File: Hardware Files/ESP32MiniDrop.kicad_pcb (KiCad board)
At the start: 2 copper layers, 74 x 54 mm, 33 parts, among them J2 Barrel_Jack, J3 AudioJack3, J4 Solenoid1 Terminal, J5 0.100" 2x4 Header, M1 Conn_01x01, M2 Conn_01x01, M3 Conn_01x01, M4 Conn_01x01, Q3 NMOS 60V 46A, SW1 SPST (RED), SW2 SPST (BLUE), U2 AZ1117-3.3, U3 ESP32-WROOM-32, U4 4N25, U5 4N25

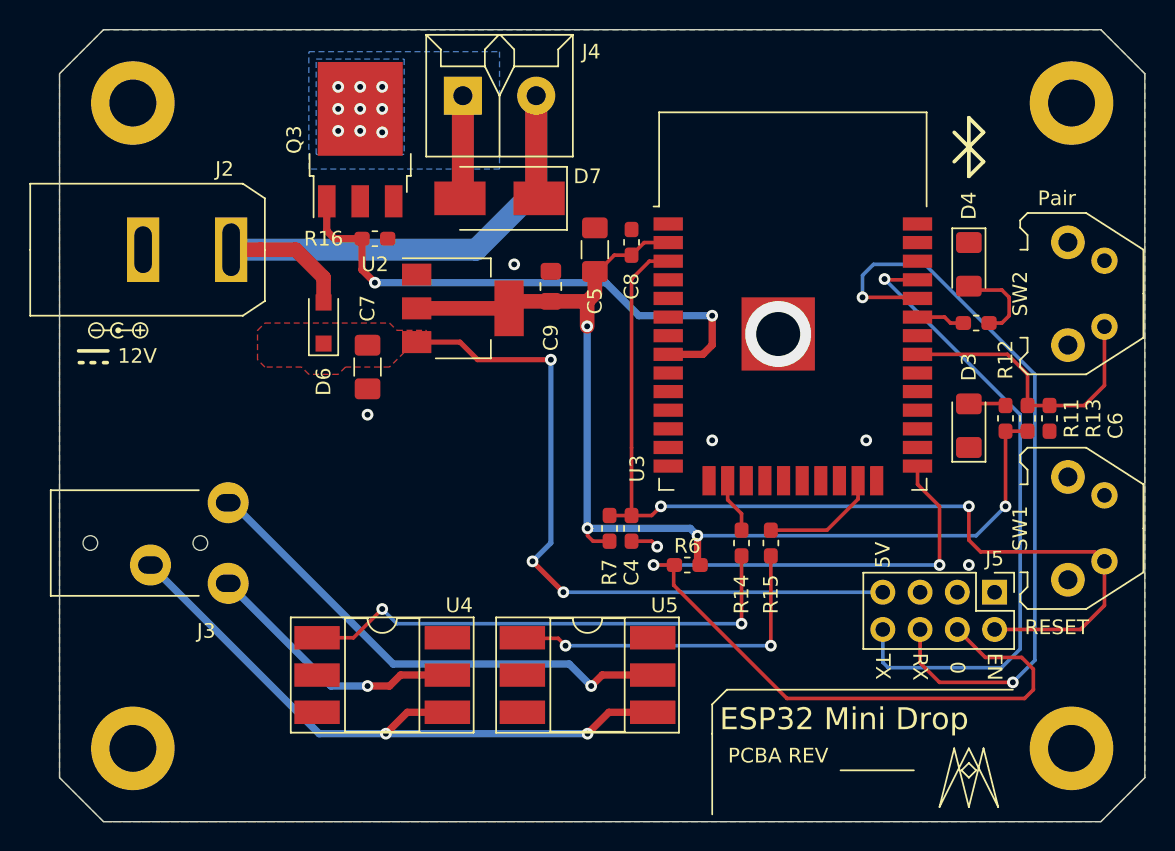
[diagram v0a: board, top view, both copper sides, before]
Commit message: Update passives to all 1206, unroute and reposition
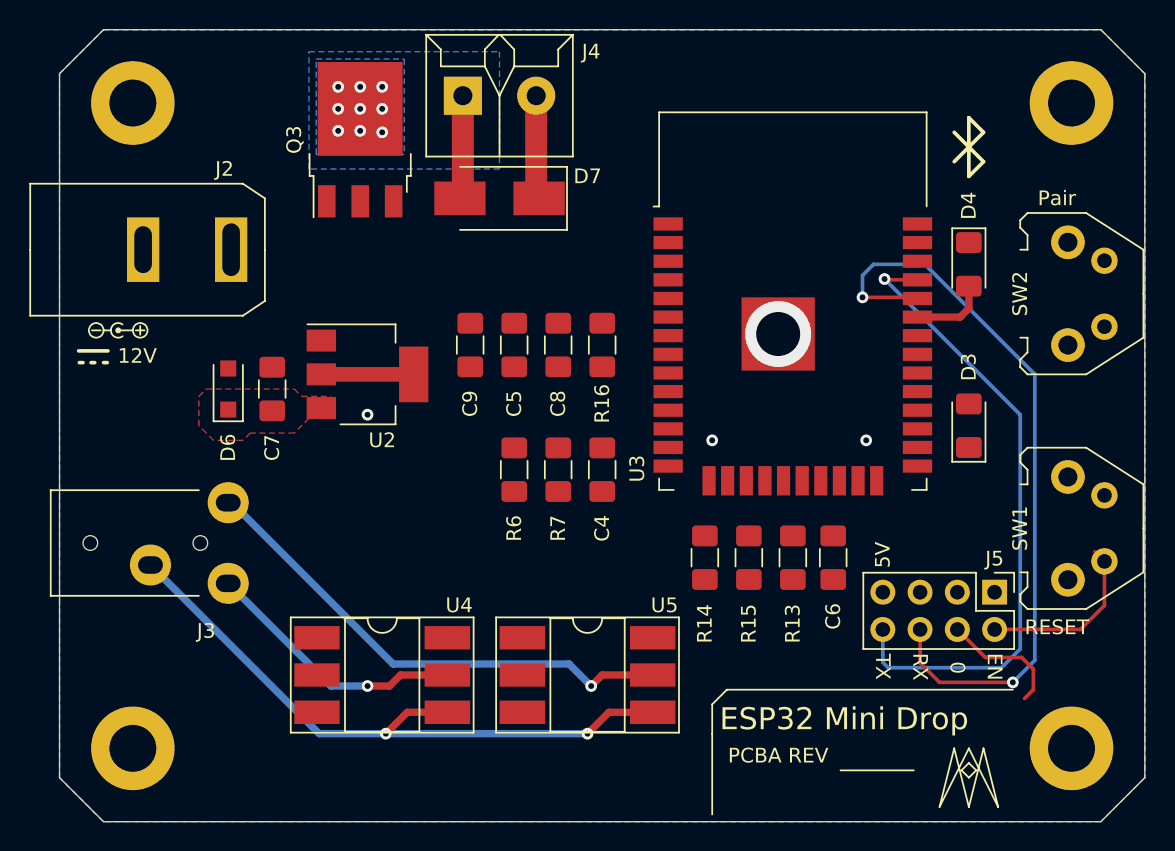
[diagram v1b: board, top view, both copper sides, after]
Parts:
- removed R11, R12: 0R 0.1W, Resistor_SMD:R_0603_1608Metric_Pad1.05x0.95mm_HandSolder
- C4, C6, C8: footprint Capacitor_SMD:C_0603_1608Metric_Pad1.05x0.95mm_HandSolder -> Capacitor_SMD:C_1206_3216Metric_Pad1.42x1.75mm_HandSolder
- C9: footprint Capacitor_SMD:C_0805_2012Metric_Pad1.15x1.40mm_HandSolder -> Capacitor_SMD:C_1206_3216Metric_Pad1.42x1.75mm_HandSolder
- R13, R14, R15, R16, R6, R7: footprint Resistor_SMD:R_0603_1608Metric_Pad1.05x0.95mm_HandSolder -> Resistor_SMD:R_1206_3216Metric_Pad1.42x1.75mm_HandSolder
- moved R13 18.6 mm to (50.0, 36.0)
- moved C6 17.5 mm to (52.8, 36.0)
- moved R16 17.1 mm to (37.0, 21.5), turned to 90 degrees
- moved R6 13.5 mm to (31.0, 30.0), turned to 270 degrees
- moved C8 8.60 mm to (34.0, 21.5)
- moved C5 8.51 mm to (31.0, 21.5)
- moved D6 7.91 mm to (11.5, 24.5)
- moved U2 7.91 mm to (21.0, 23.5)
- moved C9 6.80 mm to (28.0, 21.5)
- moved C7 6.67 mm to (14.5, 24.5), turned to 270 degrees
- moved R7 5.32 mm to (34.0, 30.0), turned to 270 degrees
- moved C4 4.47 mm to (37.0, 30.0), turned to 270 degrees
- moved R14 2.69 mm to (44.0, 36.0)
- moved R15 1.80 mm to (47.0, 36.0)
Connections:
- D3 pad 2: Net-(D3-Pad2) -> +3V3
- D4 pad 2: Net-(D4-Pad2) -> PairLED_CTLO
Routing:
- net +3V3: track 76.0 -> 6.83 mm, vias 4 -> 0
- net /IO0: track 65.4 -> 8.56 mm, vias 2 -> 0
- net /EN: track 67.2 -> 12.1 mm, vias 2 -> 0
- net /VREG_IN: track 49.1 -> 0.30 mm, vias 3 -> 0
- net +12V: track 45.1 -> 7.37 mm
- net Solenoid_1_CTLO: track 37.4 -> 0.00 mm, vias 2 -> 0
- net Net-(R14-Pad1): track 34.8 -> 0.00 mm, vias 2 -> 0
- net Net-(R15-Pad1): track 23.3 -> 0.06 mm, vias 2 -> 0
- net PairSwitch_CTLI: track 20.2 -> 0.16 mm
- net Shutter_CTLO: track 8.07 -> 0.00 mm
- net Net-(D4-Pad2): track 6.05 -> 0.00 mm
- net Focus_CTLO: track 3.76 -> 0.00 mm
- net Net-(D3-Pad2): track 2.56 -> 0.00 mm
- net PairLED_CTLO: track 3.29 -> 5.52 mm
- net GND: track 1.91 -> 0.00 mm, vias 7 -> 4

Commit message: Reroute components
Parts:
- added R1: 10k 1% 0.1W, Resistor_SMD:R_1206_3216Metric_Pad1.42x1.75mm_HandSolder, F.Cu at (40.0, 38.0)
- moved U5 16.9 mm to (22.0, 34.5), turned to 180 degrees
- moved R14 7.28 mm to (37.0, 38.0)
- moved C6 4.47 mm to (48.8, 38.0)
- moved R13 4.47 mm to (46.0, 38.0)
- moved R15 4.47 mm to (43.0, 38.0)
- moved U4 1.00 mm to (22.0, 45.0), turned to 180 degrees
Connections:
- U3 pad 23: Shutter_CTLO -> U0TX_Active
- U3 pad 24: Net-(U3-Pad24) -> Shutter_CTLO
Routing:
- net /EN: track 12.1 -> 83.9 mm, vias 0 -> 3
- net /IO0: track 8.56 -> 80.2 mm, vias 0 -> 4
- net +3V3: track 6.83 -> 78.2 mm, vias 0 -> 7
- net /VREG_IN: track 0.30 -> 71.2 mm, vias 0 -> 2
- net PairSwitch_CTLI: track 0.16 -> 41.7 mm, vias 0 -> 2
- net Solenoid_1_CTLO: track 0.00 -> 31.1 mm
- net Net-(J3-PadT): track 34.4 -> 7.24 mm, vias 1 -> 0
- net U0TX_Active: track 0.00 -> 26.3 mm, vias 0 -> 2
- net Net-(R14-Pad1): track 0.00 -> 21.4 mm, vias 0 -> 2
- net Net-(R15-Pad1): track 0.06 -> 21.1 mm
- net Shutter_CTLO: track 0.00 -> 17.5 mm
- net Net-(J3-PadS): track 44.4 -> 27.4 mm
- net Focus_CTLO: track 0.00 -> 13.5 mm
- net +12V: track 7.37 -> 15.5 mm
- net Net-(J3-PadR): track 18.2 -> 17.5 mm, vias 1 -> 0
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- added copper zone on B.Cu, net +12V
- added copper zone on F.Cu, net +3V3

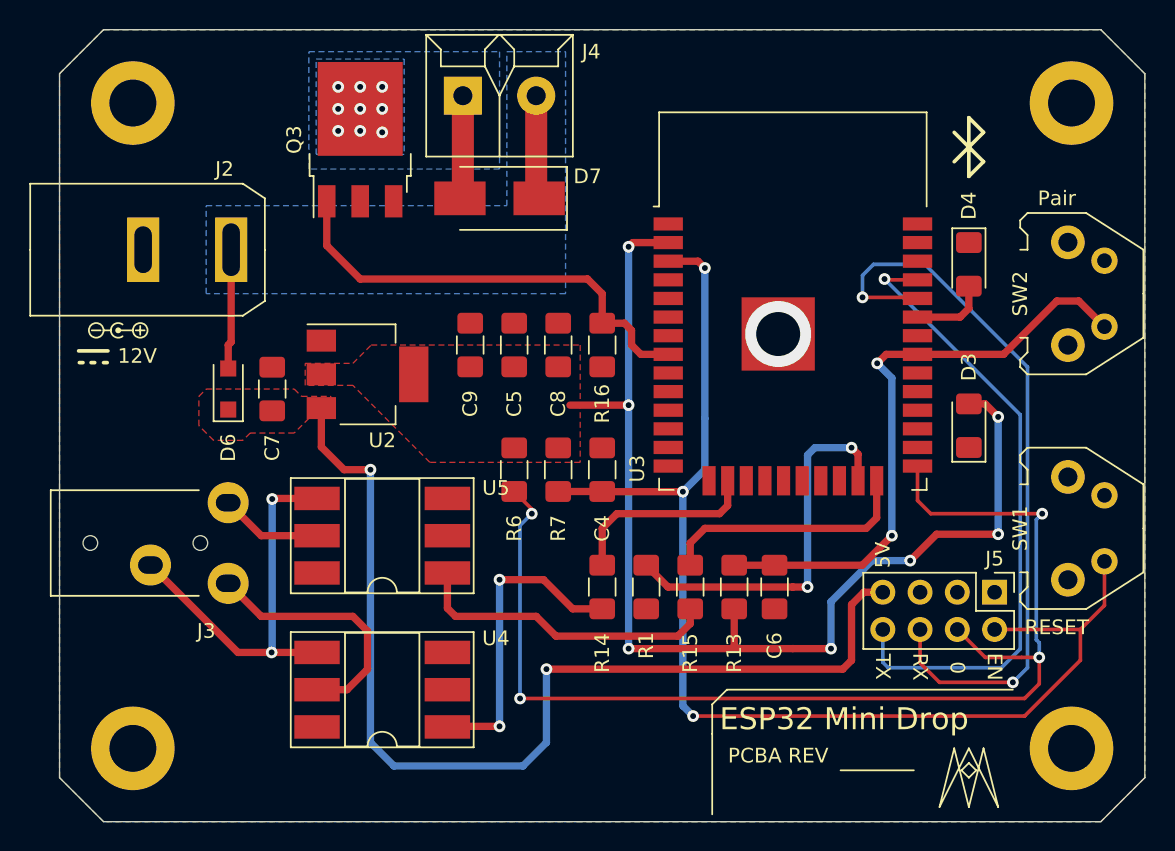
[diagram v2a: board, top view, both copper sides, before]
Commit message: Attach Pair Switch to ESP32 IO0 for boot mode selection
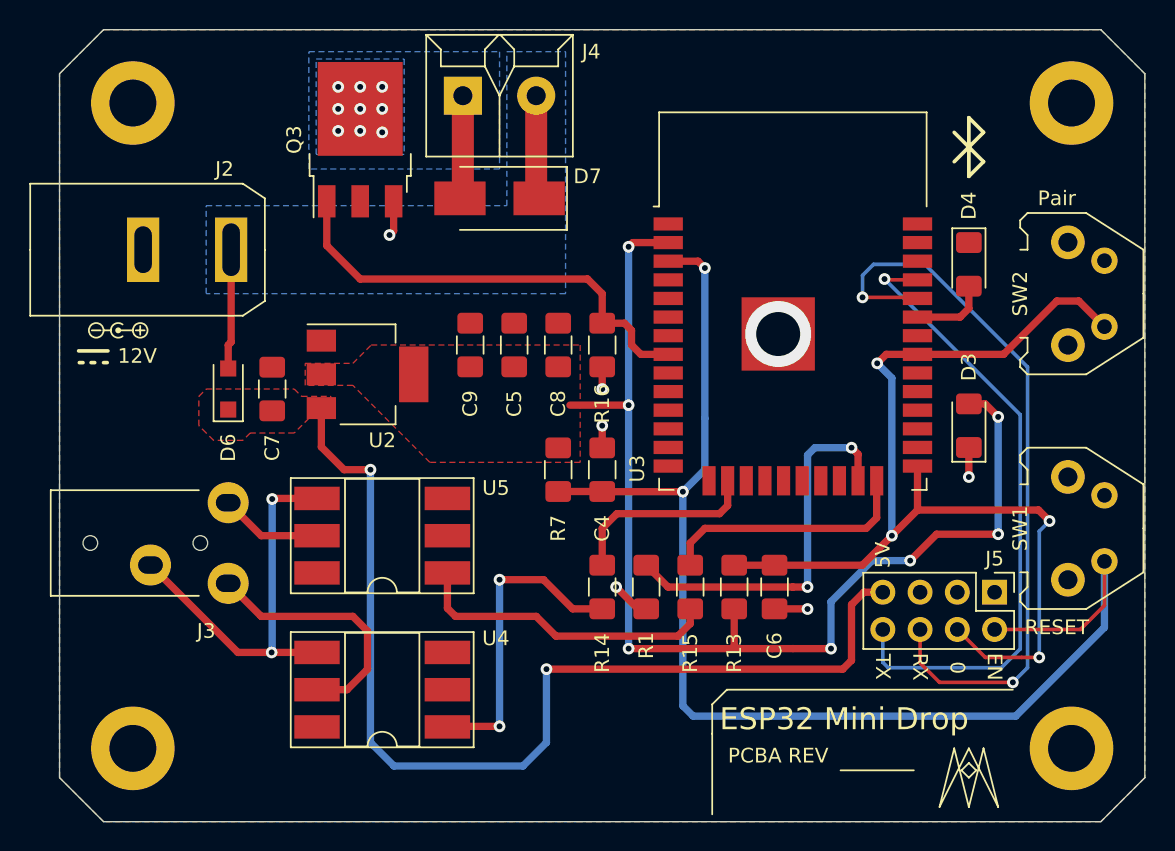
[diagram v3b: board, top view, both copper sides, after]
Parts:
- removed R6: 10k 1% 0.1W, Resistor_SMD:R_1206_3216Metric_Pad1.42x1.75mm_HandSolder
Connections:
- J5 pad 4: /IO0 -> PairSwitch_CTLI
- U3 pad 25: /IO0 -> PairSwitch_CTLI
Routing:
- net /IO0: track 80.2 -> 0.00 mm, vias 4 -> 0
- net PairSwitch_CTLI: track 41.7 -> 74.8 mm, vias 2 -> 4
- net GND: track 0.00 -> 12.4 mm, vias 1 -> 7
- net /EN: track 83.9 -> 88.9 mm, vias 3 -> 2

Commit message: Update Component MPN and Values
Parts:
- removed C9: 22uF 6.3V, Capacitor_SMD:C_1206_3216Metric_Pad1.42x1.75mm_HandSolder
- C2: renamed from C5; value 10uF 50V -> 10uF 25V 10%
- C5: renamed from C7; value 10uF 50V -> 10uF 25V 10%
- renumbered C4 to C1, C8 to C3, C6 to C4, D3 to D1, D4 to D2, D7 to D3, D6 to D4, J5 to J1, J4 to J2, J2 to J4, Q3 to Q1, R7 to R1, R13 to R2, R1 to R3, R14 to R4, R16 to R5, R15 to R6, SW2 to SW1, SW1 to SW2, U3 to U1, U4 to U2, U5 to U3, U2 to U4

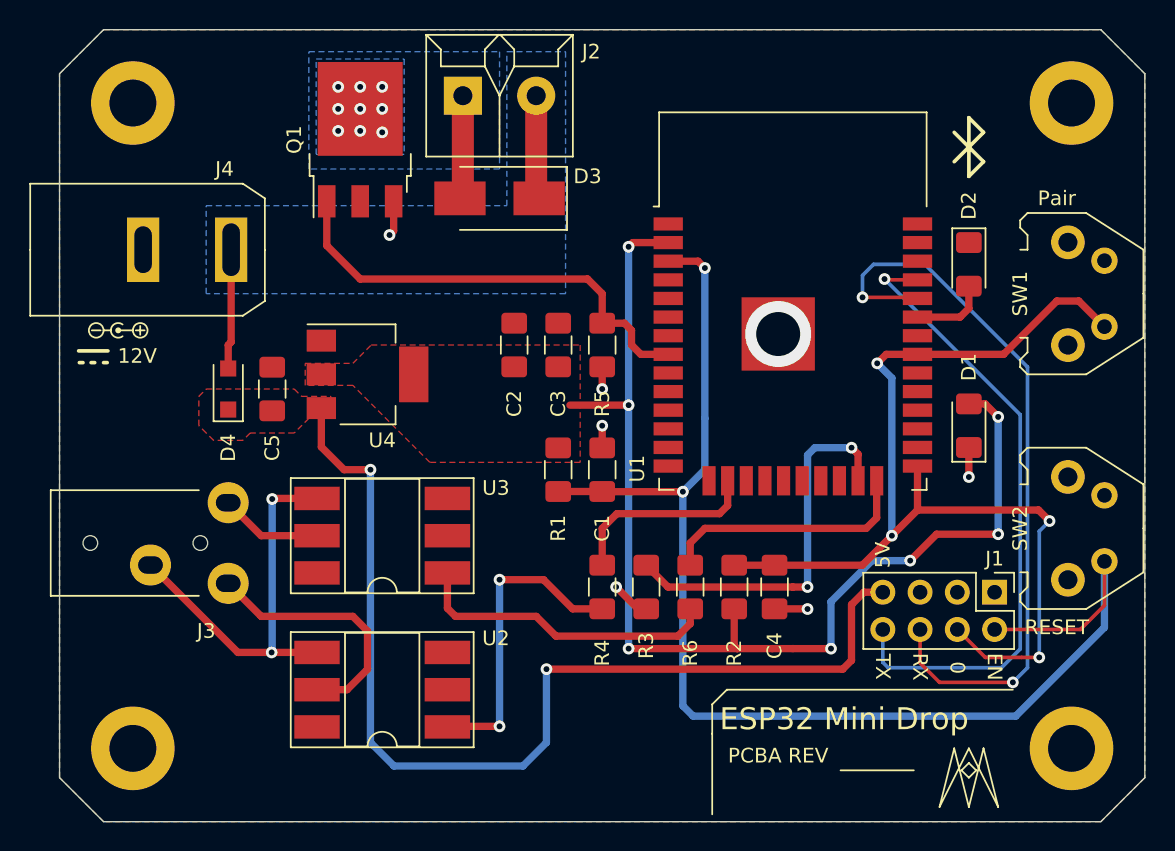
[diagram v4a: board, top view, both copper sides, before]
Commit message: Change barrel jack part, update routing
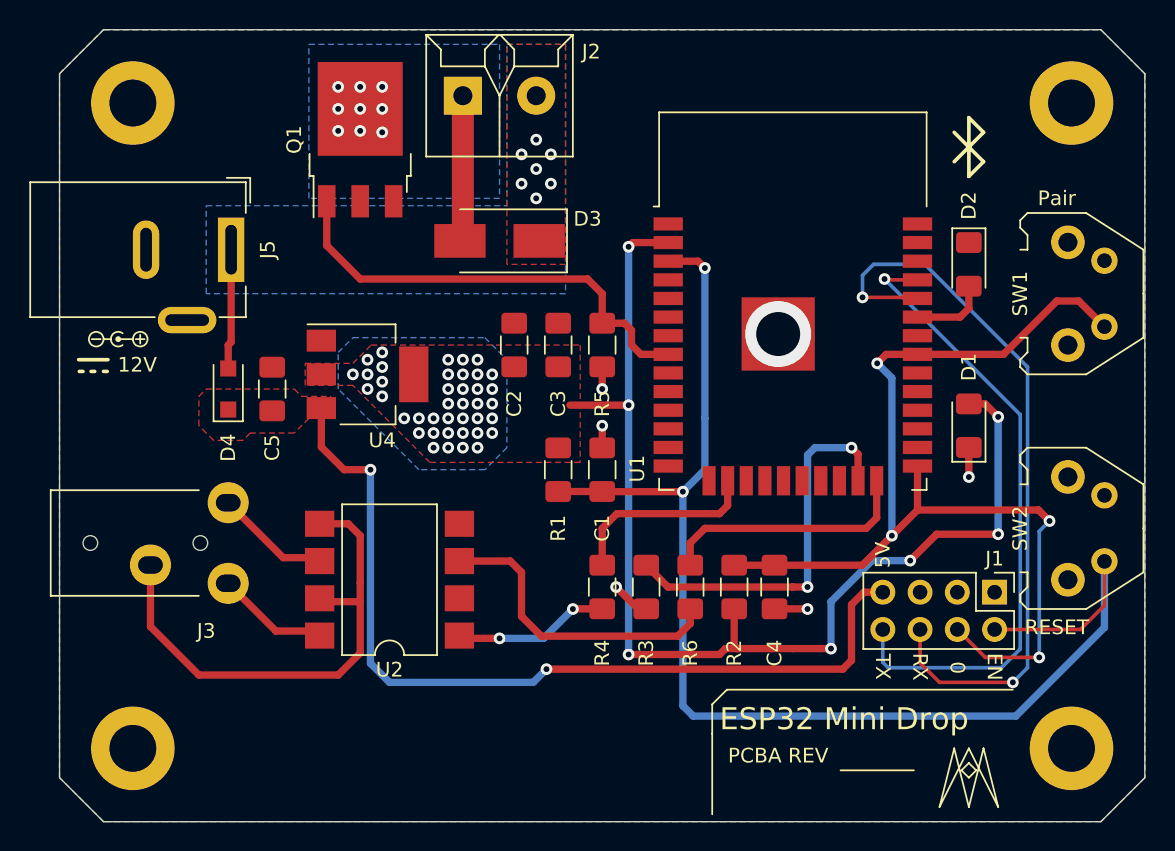
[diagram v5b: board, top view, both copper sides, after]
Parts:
- removed J4: Barrel_Jack, ESP32MiniDrop_PCB_Library:PJ-037A
- removed U3: 4N25, Package_DIP:DIP-6_W8.89mm_SMDSocket_LongPads
- added J5: Barrel_Jack_Switch, ESP32MiniDrop_PCB_Library:BarrelJack_Wuerth_6941xx301002_3D, F.Cu at (11.7, 15.0)
- R1, R2, R3, R5: value 10k 1% 0.1W -> 10k 5% 0.25W
- R4, R6: value 220R 1% 0.1W -> 220R 5% 0.25W
- U2: value 4N25 -> LTV-827S; footprint Package_DIP:DIP-6_W8.89mm_SMDSocket_LongPads -> Package_DIP:SMDIP-8_W9.53mm
- moved U2 7.52 mm to (22.5, 37.5)
- moved D3 2.90 mm to (30.0, 14.4)
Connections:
- U2 pad 3: Net-(U2-Pad3) -> Net-(R6-Pad1)
- U2 pad 4: Net-(J3-PadS) -> GND
- U2 pad 5: Net-(J3-PadR) -> Net-(J3-PadS)
- U2 pad 6: Net-(U2-Pad6) -> Net-(J3-PadT)
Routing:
- net /VREG_IN: track 71.2 -> 60.4 mm
- net Net-(R4-Pad1): track 21.4 -> 10.7 mm
- net Net-(J3-PadR): track 17.5 -> 7.71 mm
- net Net-(J3-PadS): track 27.4 -> 34.4 mm, vias 2 -> 0
- net +12V: track 15.5 -> 8.75 mm, vias 0 -> 7
- net GND: track 12.4 -> 9.96 mm, vias 7 -> 6
- net Net-(D3-Pad2): track 8.38 -> 9.98 mm
- net Net-(J3-PadT): track 7.24 -> 8.13 mm
- net +3V3: track 78.2 -> 78.8 mm, vias 7 -> 47
- added copper zone on F.Cu, net +12V
- added copper zone on B.Cu, net +3V3
- removed copper zone on B.Cu, net Solenoid_1_CTLO
